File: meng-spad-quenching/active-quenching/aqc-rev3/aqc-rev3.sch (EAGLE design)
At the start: 299 parts, among them IC1 TPS7A4901, IC10 TPS7A3001, IC11 LT1534-1, IC12 74AHC1G04DBV, IC13 74AHC1G04DBV, IC14 NC7WZ16P6X, IC15 LTC1711, IC16 TLV272DGK, IC17 TLV271DBV, IC18 USBLC6-2SC6Y, IC19 ALD1107, IC2 TPS7A4901, IC20 ALD1106, IC21 STM32F411RE, IC22 MAX572X, IC23 TLV271DBV, IC24 LM1117, IC3 LT1534-1, IC4 74AHC1G04DBV, IC5 ADCMP582, IC6 DS1100LU-20+, IC7 74AHC1G04DBV, IC8 NC7SV74K8X, IC9 TLV272DGK, M1 BSS806N, M2 BSS806N, M3 BSS806N, Q1 MMBTH81, Q2 MMBTH81, Q3 MMBTH81, Q4 MMBTH81, Q5 MMBTH81, Q6 IRLML6402TRPBF, SW1 MCU_RST, T1 MMBTH10, T2 MMBTH10, T3 MMBTH10, T4 MMBTH10, T5 MMBTH10, T6 MMBTH10, T7 MMBTH10, U1 MCP4725, U2 SN65EPT22DGK, U3 SN65EPT21DGK, X1 CONN_PULLDN_SENSE, X2 CONN_FORCE_QUENCH, X3 KEYSTONE-7774, X4 CONN_SPAD, X5 CONN_PHOTON_COUNTER, X6 KEYSTONE-7774, X7 CONN_SMU, X8 PN61729-S

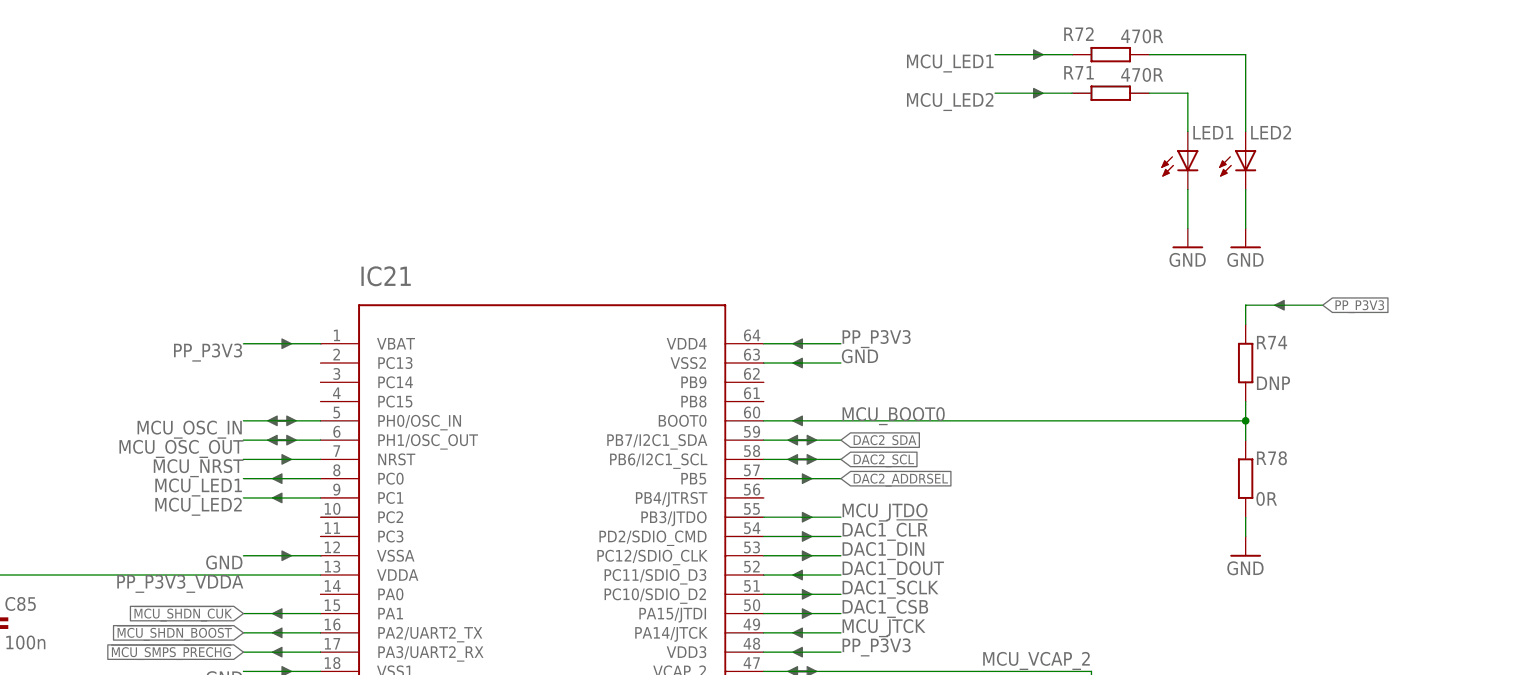
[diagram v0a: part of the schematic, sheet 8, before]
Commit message: Started plant raman, aqc-rev3, and sense1 wirebonder
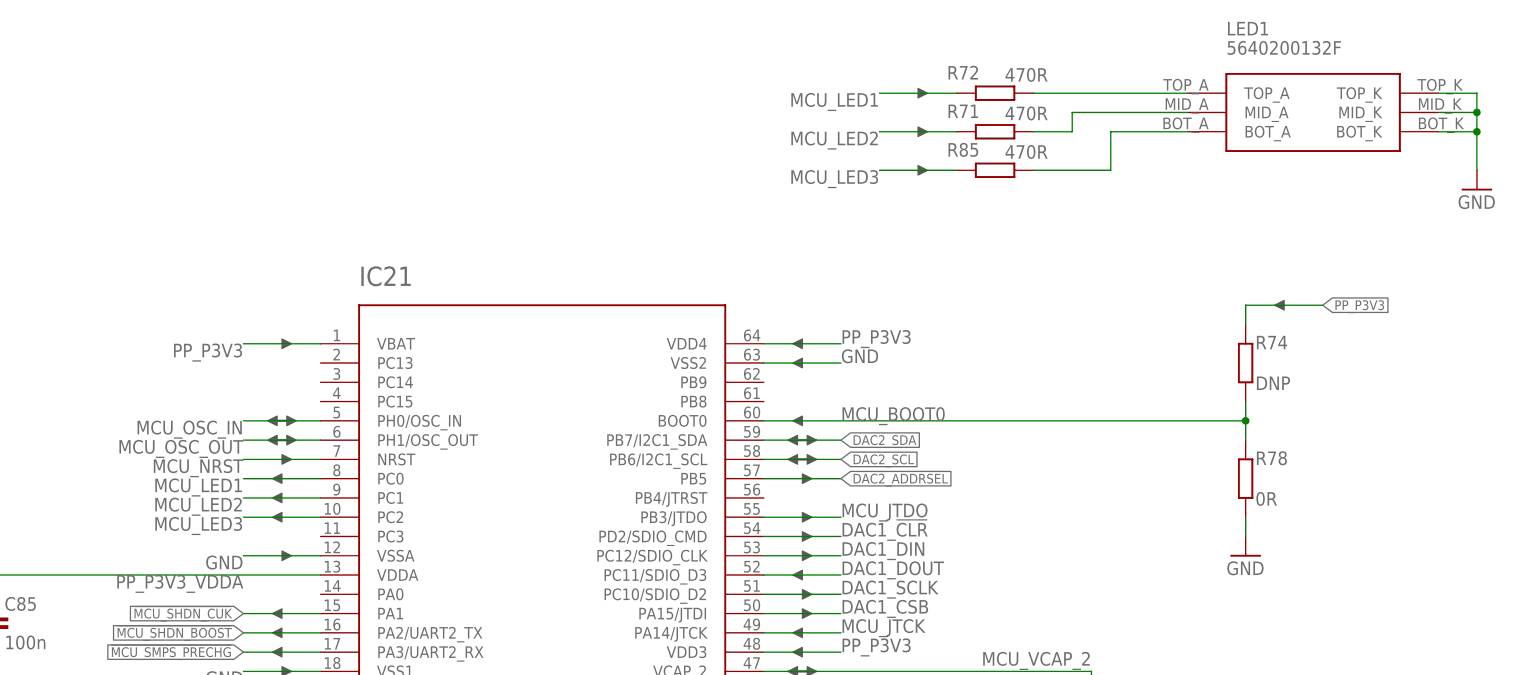
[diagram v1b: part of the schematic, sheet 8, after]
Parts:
- removed LED2: (no value), led:LEDCHIP-LED0805
- added D9: (no value), diode:DIODE-SOD523
- added R85: 470R, resistor:R-EU_R0603
- LED1: value (none) -> 5640200132F; device led:LEDCHIP-LED0805 -> meng:CBI-564-0X00-XXX-3LED
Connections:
- new net MCU_LED3: IC21.PC2, R85.2
- new net N$31: LED1.BOT_A, R85.1
- net GND: now also D9.A, LED1.BOT_K, LED1.MID_K, LED1.TOP_K; no longer LED1.C, LED2.C
- net N$24: now also LED1.MID_A; no longer LED1.A
- net N$9: now also LED1.TOP_A; no longer LED2.A
- net V_SPAD: now also D9.C
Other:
- moved on the sheet: R71, R72

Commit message: Work on new leaf heater and AQC with new BJTs, level shift topology
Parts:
- removed C19, C48, C50, C87, C89: 100n, rcl:C-EUC0402
- removed C20, C47, C49, C88, C90: 10n, rcl:C-EUC0402
- removed C28, C65: 470p, rcl:C-EUC0603
- removed C29, C73: 10p, rcl:C-EUC0603
- removed C43, C64: 100n, rcl:C-EUC0603
- removed C83: 47u, 20V, rcl:CPOL-EUCT7343
- removed D2, D3, D5, D6: BAS40, diode:BAS40
- removed Q1, Q2, Q3, Q4, Q5: MMBTH81, transistor-pnp:MMBTH81LT1SMD
- removed R27, R31, R42, R57: DNP, rcl:R-EU_R0603
- removed R28, R33, R60: 0R, rcl:R-EU_R0603
- removed R36, R37, R51, R64, R68: 470R, rcl:R-EU_R0603
- removed R44, R45, R69, R70: 100k, rcl:R-EU_R0603
- removed R50: 49R9, rcl:R-EU_R0603
- removed T1, T2, T3, T4, T5, T6, T7: MMBTH10, transistor:MMBTH10LT1-NPN-SOT23-BEC
- added IC25: HFA3134, meng:HFA3134
- added IC26: THAT320, meng:THAT320
- C1, C10, C11, C17, C18, C2, C45, C5, C52, C55, C57, C58, C59, C6, C7, C71, C72, C8, C9: device rcl:C-EUC0603 -> rcl-modified-footprints:C-EUC0603
- C32, C33: device rcl:C-EUC0402 -> rcl-modified-footprints:C-EUC0402
- C56: value 10n -> 100p; device rcl:C-EUC0603 -> rcl-modified-footprints:C-EUC0402
- IC13: value 74AHC1G04DBV -> TLV271DBV; device 74xx-little-de:74AHC1G04DBV -> meng:TLV271DBV
- IC16, IC9: value TLV272DGK -> HFA3134; device meng:TLV272DGK -> meng:HFA3134
- IC17: value TLV271DBV -> HFA3135; device meng:TLV271DBV -> meng:HFA3135
- IC19: value ALD1107 -> HFA3135; device meng:ALD1107 -> meng:HFA3135
- IC20: value ALD1106 -> HFA3134; device meng:ALD1106 -> meng:HFA3134
- IC23: value TLV271DBV -> HFA3134; device meng:TLV271DBV -> meng:HFA3134
- IC4: value 74AHC1G04DBV -> TLV272DGK; device 74xx-little-de:74AHC1G04DBV -> meng:TLV272DGK
- IC7: value 74AHC1G04DBV -> HFA3134; device 74xx-little-de:74AHC1G04DBV -> meng:HFA3134
- L4: value SRF0703-820M -> 732-1699-2-ND; device meng:SRF0703 -> meng:WE_INDUCTOR; VALUE SRF0703 -> (none)
- R1, R12, R13, R2, R3, R38, R4, R40, R5, R6, R7: device resistor:R-EU_R0603 -> rcl-modified-footprints:R-EU_R0603
- R10, R11, R14, R17, R18, R19, R20, R21, R41, R56: device rcl:R-EU_R0603 -> rcl-modified-footprints:R-EU_R0603
- R26: value DNP -> 220R; device rcl:R-EU_R0603 -> rcl-modified-footprints:R-EU_R0603
- R32: value 1k -> 220R; device rcl:R-EU_R0603 -> rcl-modified-footprints:R-EU_R0603
- R43, R59: value 200R -> 220R; device rcl:R-EU_R0603 -> rcl-modified-footprints:R-EU_R0402
- R46, R49: device rcl:R-EU_R0603 -> rcl-modified-footprints:R-EU_R0402
- TP20: value DELAY_UP -> (DELAY_UP)
- TP21: value DELAY_DN -> (DELAY_DN)
- X1, X2, X4, X5, X7: device meng:SMA-142-0711-871/876 -> meng:SMA-142-0701-881/886
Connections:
- net VREF_CASCODE_IBIAS renamed VREF_DELTAV_SETPOINT
- removed net CASC_BIAS_B: IC17.OUT, T6.B
- removed net CASC_BIAS_C: R64.2, T5.E, T6.C
- removed net CASC_BIAS_E: R65.2, R73.1, T6.E
- removed net CASC_BIAS_VGND: IC17.-IN, R73.2, R81.1
- removed net CASC_MIDPT: T4.E, T5.C
- removed net DELAY_CAP: C29.1, IC4A.I, IC7A.O
- removed net DIAMOND_IBIAS_NMOS: C57.2, IC20_M4.D, Q3.B, R43.1
- removed net DIAMOND_IBIAS_PMOS: C57.1, IC19_M4.D, R59.2, T3.B
- removed net LBOOST_!: L4.2, L4.3
- removed net N$1: IC16_A.-IN, Q4.E, R51.1
- removed net N$17: D6.C, IC13P.GND, T7.C
- removed net N$2: R57.1, R60.1, T5.B
- removed net N$21: Q5.B, R50.1, T2.B
- removed net N$22: R50.2, R56.1, T4.C
- removed net N$27: Q2.C, R32.2, R33.2, R42.1
- removed net N$32: R26.1, R28.1, X1G1.1
- removed net N$38: IC16_A.OUT, Q4.B
- removed net N$42: IC16_B.OUT, T7.B
- removed net N$43: IC16_B.-IN, R69.2, R70.1
- removed net N$44: D2.A, IC7P.VCC, Q1.C
- removed net N$45: D3.C, IC7P.GND, T1.C
- removed net N$46: IC9_B.OUT, T1.B
- removed net N$47: IC9_B.-IN, R44.2, R45.1
- removed net N$48: IC9_A.-IN, Q1.E, R37.1
- removed net N$49: IC9_A.OUT, Q1.B
- removed net N$50: IC20_M1.S, IC23.-IN, R80.TOP
- removed net N$7: D5.A, IC13P.VCC, Q4.C
- removed net N$78: IC20_M1.G, IC20_M2.G, IC23.OUT
- removed net N$81: IC20_M2.S, R80.BOTTOM
- removed net N$82: R68.2, R69.1, T7.E
- removed net N$86: R36.2, R44.1, T1.E
- removed net N$90: IC19_M3.D, IC19_M3.G, IC19_M4.G, IC20_M3.D
- removed net NC_IC15_V+: IC20_NC_V+.NC
- removed net NC_IC16_V-: IC19_NC_V-.NC
- removed net QUENCH_WFM: C73.1, IC13A.O, R60.2
- removed net VREF_DELAY_DN: IC22.OUT7, R45.2, TP21.P$1
- removed net VREF_DELAY_UP: IC22.OUT6, IC9_A.+IN, TP20.P$1
- removed net VREF_SLEW_DN: IC22.OUT4, R70.2, TP18.P$1
- removed net VREF_SLEW_MAX: C65.1, D5.C, IC22.OUT5, TP19.P$1
- removed net VREF_SLEW_UP: IC16_A.+IN, IC22.OUT3, TP17.P$1
- new net CCS_STEERING_TAIL: IC20_Q1.E, IC20_Q2.E, IC25_Q1.C
- new net CCS_VA_SETPOINT: IC23_Q2.E, IC25_Q2.C
- new net DELTAV_BASE: IC25_Q1.B, IC4_A.OUT
- new net DELTAV_FB: IC25_Q1.E, R65.2, R73.1
- new net DELTAV_VGND: IC4_A.-IN, R73.2, R81.1
- new net DIAMOND_BASE: IC13.OUT, IC7_Q1.B, IC7_Q2.B
- new net DIAMOND_FB: IC13.-IN, IC7_Q1.E, R80.TOP
- new net DIAMOND_FB_R: IC7_Q2.E, R80.BOTTOM
- new net DIAMOND_IBIAS_BOTTOM: C57.2, IC17_Q2.B, IC9_Q2.C, R43.1
- new net DIAMOND_IBIAS_MID: IC26Q3.B, IC26Q4.B, IC26Q4.C, IC9_Q1.C
- new net DIAMOND_IBIAS_TOP: C57.1, IC16_Q2.B, IC26Q3.C, R59.2
- new net DIAMOND_IN: IC16_Q1.B, IC17_Q1.B, IC23_Q1.C, IC23_Q2.C, R56.1
- new net N$30: IC17_Q1.C, IC19_Q1.E
- new net N$35: IC20_Q2.C, IC23_Q1.E
- new net VA_BASE: IC25_Q2.B, IC4_B.OUT
- new net VA_FB: IC25_Q2.E, IC4_B.-IN, R26.2
- new net VREF_EXTRA_1: IC22.OUT4, TP18.P$1
- new net VREF_EXTRA_2: IC22.OUT5, TP19.P$1
- new net VREF_EXTRA_3: IC22.OUT6, TP20.P$1
- new net VREF_EXTRA_4: IC22.OUT7, TP21.P$1
- new net VREF_VA_SETPOINT: IC22.OUT3, IC4_B.+IN, TP17.P$1
- net !LOGIC_QUENCH: now also IC20_Q1.B; no longer IC13A.I
- net BLANKING_LATCH_EN: no longer IC4A.O
- net BOOST_SW_NODE: now also L4.P$2; no longer L4.4
- net GND: now also IC13.V-, IC19_Q1.C, IC26SUBC.SUBC, IC4_A.+IN, R26.1; no longer C19.2, C20.2, C28.2, C29.2, C43.2, C47.2, C48.2, C49.2, C50.2, C64.2, C65.2, C73.2, C83.-, C87.2, C88.2, C89.2, C90.2, D3.A, D6.A, IC16_B.+IN, IC17.+IN, IC20_SUBC_V-.SUBC, IC23.V-, IC4P.GND, IC9_B.+IN, Q5.C, R27.1, R31.1
- net LOGIC_QUENCH: now also IC20_Q2.B; no longer IC7A.I, R57.2
- net N$10: now also IC17_Q2.C, IC19_Q2.E; no longer Q2.E, Q3.C, R42.2
- net N$11: now also IC17_Q1.E; no longer Q5.E
- net N$13: now also IC16_Q1.E; no longer T2.E
- net N$14: now also IC17_Q2.E; no longer Q3.E
- net N$16: now also IC7_Q1.C, IC9_Q1.E; no longer IC20_M1.D, IC20_M3.S
- net N$26: now also IC7_Q2.C, IC9_Q2.E; no longer IC20_M2.D, IC20_M4.S
- net N$28: now also X1G1.1; no longer R28.2, R31.2
- net N$5: now also IC16_Q2.E; no longer T3.E
- net N$88: now also IC26Q1.B, IC26Q1.C, IC26Q2.B, IC26Q4.E; no longer IC19_M1.D, IC19_M1.G, IC19_M2.G, IC19_M3.S
- net N$89: now also IC26Q2.C, IC26Q3.E; no longer IC19_M2.D, IC19_M4.S
- net PP_N5V0_ANALOG: now also IC4_A.V-; no longer C47.1, C48.1, C87.1, C88.1, IC16_A.V-, IC17.V-, IC9_A.V-, R36.1, R64.1, R68.1
- net PP_P15V0_ANALOG: now also IC16_Q1.C, IC16_Q2.C, IC26Q1.E, IC26Q2.E; no longer C83.+, IC19_M1.S, IC19_M2.S, IC19_SUBC_V+.SUBC, T2.C, T3.C
- net PP_P3V3: no longer C19.1, C20.1, C28.1, D2.C, IC4P.VCC
- net PP_P5V0_ANALOG: now also IC13.V+, IC19_Q1.B, IC19_Q2.B, IC20_Q1.C, IC23_Q1.B, IC23_Q2.B, IC4_A.V+, IC9_Q1.B, IC9_Q2.B; no longer C43.1, C49.1, C50.1, C64.1, C89.1, C90.1, IC16_A.V+, IC17.V+, IC20_M3.G, IC20_M4.G, IC23.V+, IC9_A.V+, Q2.B, R37.2, R51.2, T4.B
- net SMPS_USB_VDD: now also L4.P$1; no longer L4.1
- net SPAD_PULLDN_SENSE: now also IC19_Q2.C, R32.2; no longer R26.2, R27.2, R33.1
- net VREF_DIAMOND_IBIAS: now also IC13.+IN; no longer IC23.+IN
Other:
- note added: "- Added 90-degree triple-LED inducator next to USB port"
- note added: "- Added TVS diode to SPAD output as an ESD precaution"
- note added: "- Adjusted position of USB connector to be 1.6mm off edge of PCB"
- note added: "- Changed SMA package to have thinner signal pad for better impedance matching"
- note added: "- Removed slew and delay generators, since we can trap ion and operate APDs as-in"
- note added: "- Switched biasing mirrors to THAT300/320 BJTs due to excessive VGS requirement in ALD MOSFET arrays"
- note added: "- Switched boost inductor to be larger to prevent saturation"
- note added: "2mA"
- note added: "4mA"
- note added: "Cascode provides speedup of bias current sensing by killing Miller cap. of bottom PNP in push-pull"
- note added: "Changelog (Rev. 3):"
- note added: "KCL Summing Junction"
- note added: "OPTIONAL SLEW GENERATOR"
- note added: "Optional Bypass 2nd stage filter"
- note added: "To CCS that sets Delta-V"
- note added: "To CCS that sets VA"
- note added: "Transistor Array Part Selection Note: Default Beta > 60 Pick "A" variant for Beta > 150 Pick "B" bariant for Beta > 300"
- note added: "WE 7447709471 FIXED IND 470UH 1.4A 560 MOHM"
- note removed: "-0.6V"
- note removed: "0V"
- note removed: "4.4V"
- note removed: "5V"
- note removed: "5V0 is lower noise than 3V3"
- note removed: "All collector currents approx. 1mA"
- note removed: "Amphenol 132289 (Digikey ACX1426-ND)"
- note removed: "Amphenol 132416 (Digikey ACX1921-ND)"
- note removed: "Bypass 2nd stage filter"
- note removed: "Cascode provides speedup of bias current sensing"
- note removed: "Film"
- note removed: "Higher cascode bias = lower Cmu of CE stage"
- note removed: "RC Filter Option"
- note removed: "SLEW AND DELAY GENERATORS"
- note removed: "SMT, Panel Mount SMA Connectors:"
- note removed: "by killing Miller cap. of bottom PNP in push-pull"

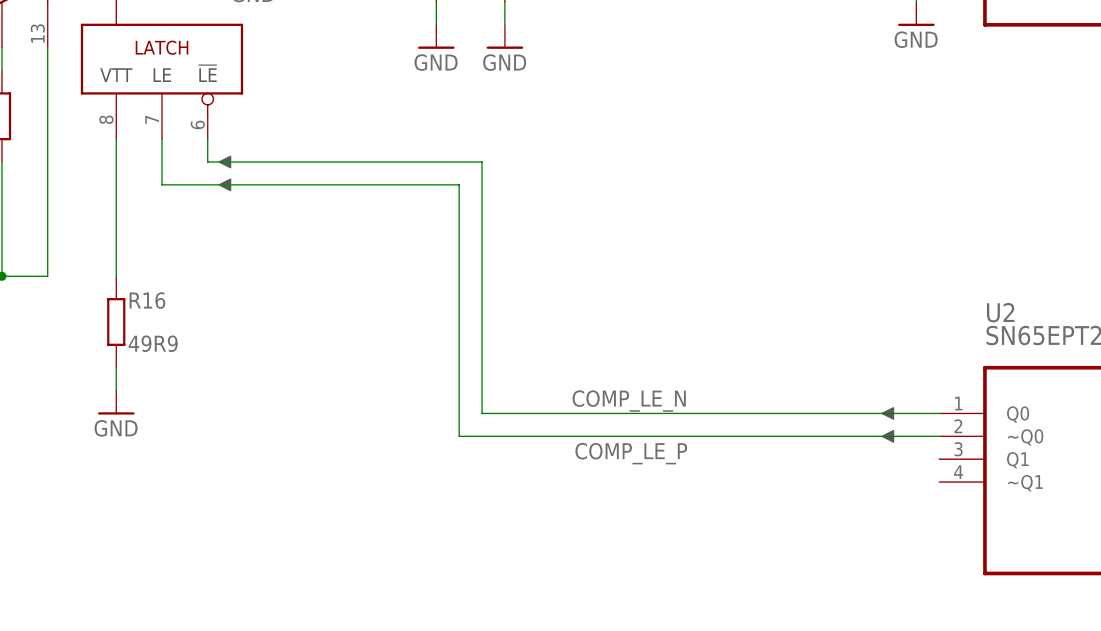
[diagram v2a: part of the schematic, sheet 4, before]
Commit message: layout work, placed and routed diamond buffer
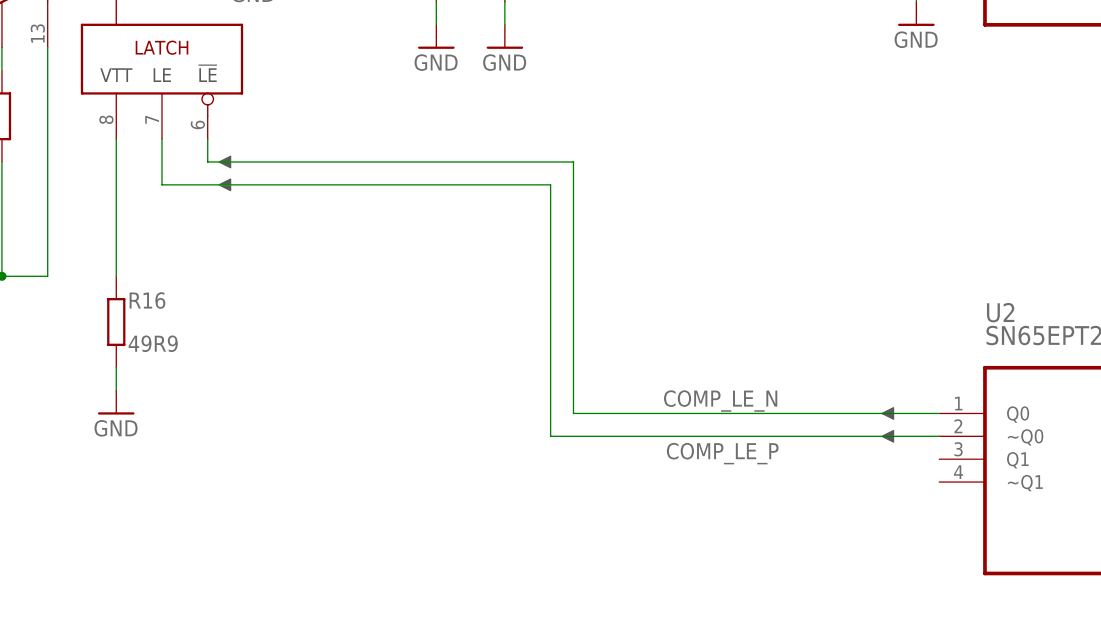
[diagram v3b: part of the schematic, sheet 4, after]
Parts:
- C21, C23, C34, C37, C38, C39: device rcl:C-EUC0402 -> rcl-modified-footprints:C-EUC0402
- C36: device rcl:C-EUC0603 -> rcl-modified-footprints:C-EUC0402
- R15, R39: device rcl:R-EU_R0603 -> rcl-modified-footprints:R-EU_R0603
- R16: device rcl:R-EU_R0603 -> rcl-modified-footprints:R-EU_R0402
- R25, R29, R30: device rcl:R-EU_R0402 -> rcl-modified-footprints:R-EU_R0402
- R41: device rcl-modified-footprints:R-EU_R0603 -> rcl-modified-footprints:R-EU_R0402
- R43, R46, R49, R59: device rcl-modified-footprints:R-EU_R0402 -> rcl-modified-footprints:R-EU_R0603
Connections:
- net N$10 renamed DMD_OP_CASC
- net N$11 renamed DMD_IN_PNP_E
- net N$13 renamed DMD_IN_NPN_E
- net N$14 renamed DMD_OP_PNP
- net N$23 renamed DMD_OUT
- net N$30 renamed DMD_IN_CASC
- net N$35 renamed STEERING_CASC
- net N$5 renamed DMD_OP_NPN
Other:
- note added: "Active-Low for Latch Mode"
- note added: "T Termination Network (50R to VTT internally from LE and !LE)"
- note removed: "T Termination Network"
